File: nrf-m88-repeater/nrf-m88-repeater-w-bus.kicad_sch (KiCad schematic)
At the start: 16 parts, among them J1 Conn_02x03_Counter_Clockwise, SW1 RESET, U1 ATmega88-20P, U2 LP2950-3.3_TO92, U3 NRF24L01_Breakout

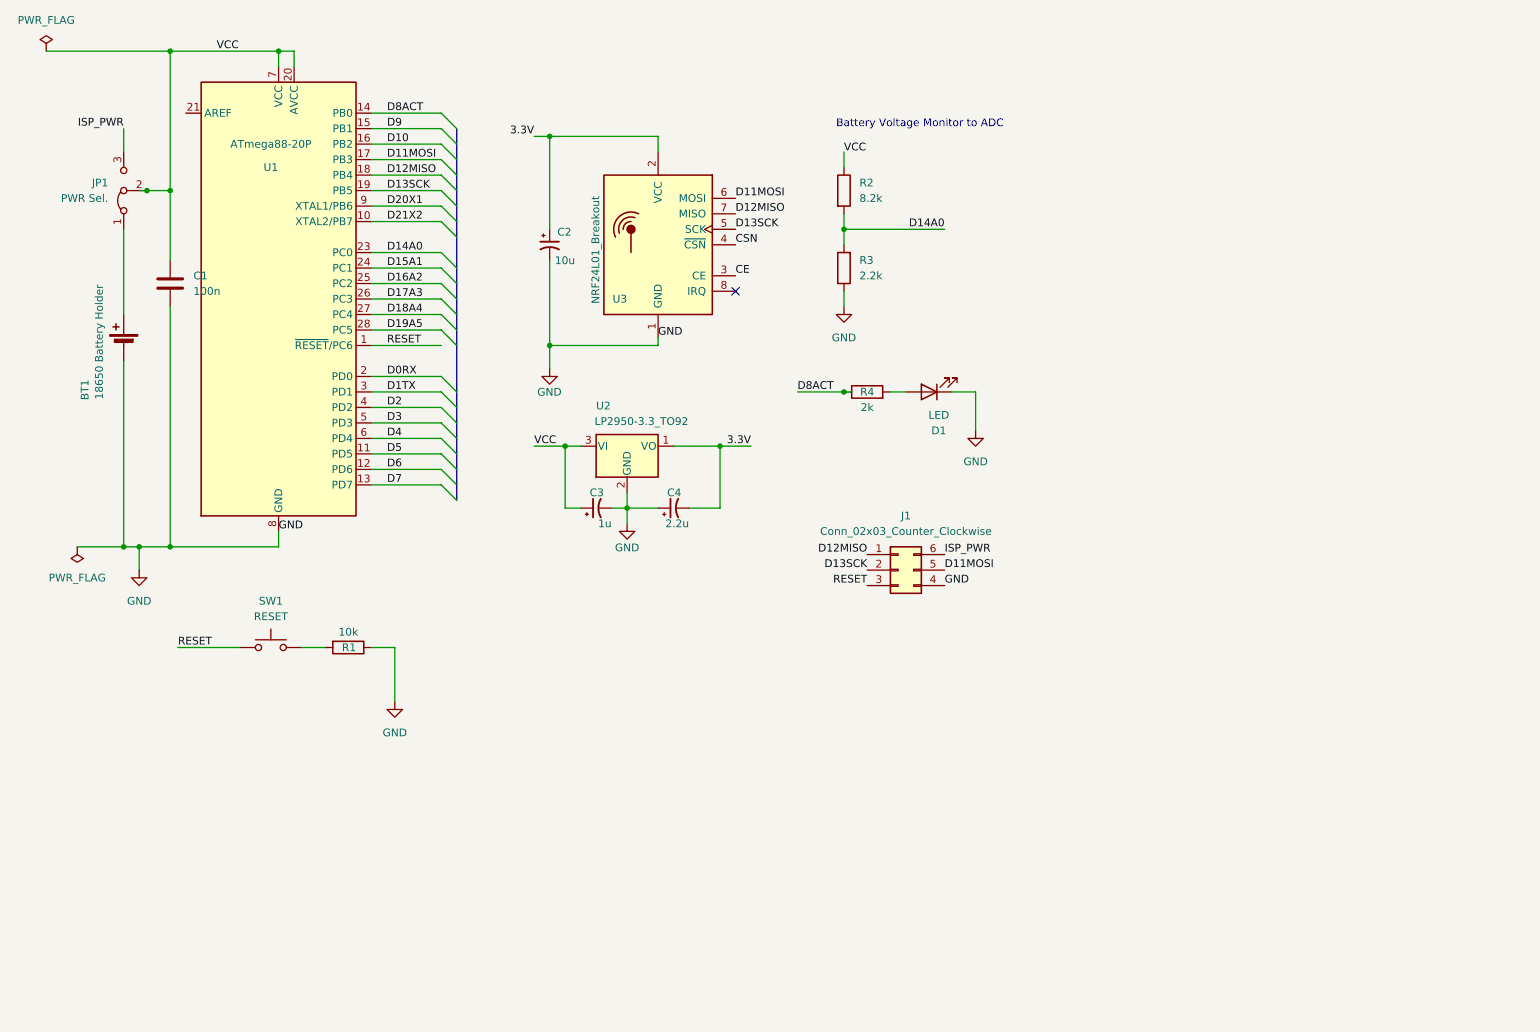
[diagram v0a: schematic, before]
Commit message: Updated Generic KiCad Model
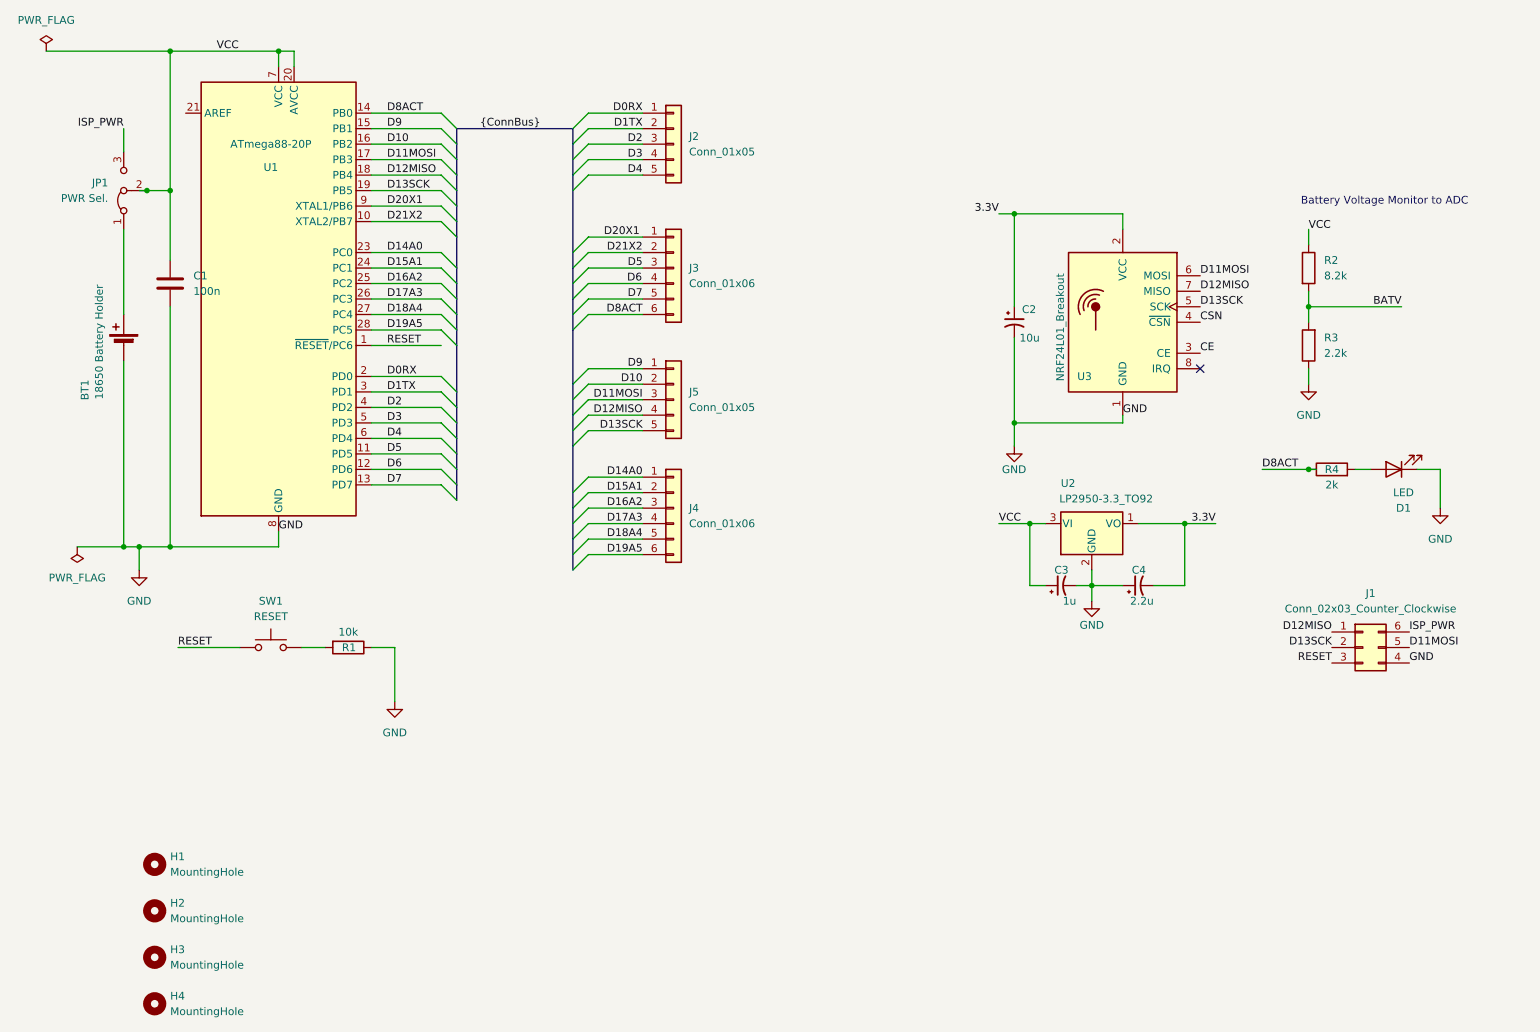
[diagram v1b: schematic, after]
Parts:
- added H1, H2, H3, H4: MountingHole, MountingHole:MountingHole_3.5mm_Pad_Via, symbol Mechanical:MountingHole
- added J2, J5: Conn_01x05, Connector_PinSocket_2.54mm:PinSocket_1x05_P2.54mm_Vertical, symbol Connector_Generic:Conn_01x05
- added J3, J4: Conn_01x06, Connector_PinHeader_2.54mm:PinHeader_1x06_P2.54mm_Vertical, symbol Connector_Generic:Conn_01x06
- R1, R2, R3, R4: footprint Resistor_SMD:R_0805_2012Metric_Pad1.20x1.40mm_HandSolder -> Resistor_THT:R_Axial_DIN0309_L9.0mm_D3.2mm_P12.70mm_Horizontal
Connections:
- net D0RX: now also J2.1 (Pin_1)
- net D10: now also J5.2 (Pin_2)
- net D11MOSI: now also J5.3 (Pin_3)
- net D12MISO: now also J5.4 (Pin_4)
- net D13SCK: now also J5.5 (Pin_5)
- net D14A0: now also J4.1 (Pin_1); no longer R2.2, R3.2
- net D15A1: now also J4.2 (Pin_2)
- net D16A2: now also J4.3 (Pin_3)
- net D17A3: now also J4.4 (Pin_4)
- net D18A4: now also J4.5 (Pin_5)
- net D19A5: now also J4.6 (Pin_6)
- net D1TX: now also J2.2 (Pin_2)
- net D2: now also J2.3 (Pin_3)
- net D20X1: now also J3.1 (Pin_1)
- net D21X2: now also J3.2 (Pin_2)
- net D3: now also J2.4 (Pin_4)
- net D4: now also J2.5 (Pin_5)
- net D5: now also J3.3 (Pin_3)
- net D6: now also J3.4 (Pin_4)
- net D7: now also J3.5 (Pin_5)
- net D8ACT: now also J3.6 (Pin_6)
- net D9: now also J5.1 (Pin_1)
- new net BATV: R2.2, R3.2
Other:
- moved on the sheet: C2, C3, C4, D1, J1, R2, R3, R4, U2, U3
